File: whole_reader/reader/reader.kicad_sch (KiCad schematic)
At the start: 59 parts, among them J1 Speaker+, J2 Speaker-, J3 Conn_02x05_Odd_Even, J4 USB_C_Receptacle_USB2.0_14P, J5 RFID RC522, J6 6P6C, SW1 SW_SPDT, SW2 SW_SPDT, U1 LM386, U2 STM32F103C8T6, U3 MCP16301Hx-xCH, U4 MAX3232, Y1 16MHz

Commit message: minor changes in pcb layout
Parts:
- removed LED1, LED2: KAA-3528SRSGS, LED_SMD:LED_PLCC-2_3x2mm_KA, symbol deadlock-reader-eagle-import:KAA-3528SRSGS
- added D7, D8: LED_Dual_AKA, LED_SMD:LED_Kingbright_KPA-3010_3x2x1mm, symbol Device:LED_Dual_AKA
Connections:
- net GND: now also D7.2 (K), D8.2 (K)
- net at R4.2: now also D7.1 (A1)
- net at R5.2: now also D7.3 (A2)
- net at R6.2: now also D8.1 (A1)
- net at R7.2: now also D8.3 (A2)

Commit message: updates of board
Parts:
- removed D4: BAT60A, Diode_SMD:D_SOD-323, symbol Device:D_Schottky_Dual_CommonAnode_AKK_Split
- added D4: BAT60A, Diode_SMD:D_SOD-323, symbol Diode:BAT60A
- U1: footprint Package_SO:MSOP-8-1EP_3x3mm_P0.65mm_EP1.73x1.85mm_ThermalVias -> Package_SO:SOIC-8_3.9x4.9mm_P1.27mm
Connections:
- net V+: now also D4.1 (K)
- net at J4.A4 (VBUS), J4.A9 (VBUS), J4.B4 (VBUS)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: now also D4.2 (A)
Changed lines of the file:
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@@
 	)
 	(junction
-		(at 212.09 157.48)
-		(diameter 0)
-		(color 0 0 0 0)
-	)
-	(junction
 		(at 238.76 45.72)
 		(diameter 0)
@@
 	(wire
 		(pts
-			(xy 222.25 157.48) (xy 212.09 157.48)
+			(xy 196.85 157.48) (xy 222.25 157.48)
 		)
 		(stroke
@@
 	(wire
 		(pts
-			(xy 212.09 157.48) (xy 196.85 157.48)
-		)
-		(stroke
-			(width 0)
-			(type default)
-		)
-	)
-	(wire
-		(pts
 			(xy 173.99 147.32) (xy 173.99 132.08)
 		)
@@
 			)
 		)
-		(property "Footprint" "Package_SO:MSOP-8-1EP_3x3mm_P0.65mm_EP1.73x1.85mm_ThermalVias"
+		(property "Footprint" "Package_SO:SOIC-8_3.9x4.9mm_P1.27mm"
 			(at 53.34 36.83 0)
 			(effects
@@
 	)
 	(symbol
+		(lib_id "Diode:BAT60A")
+		(at 226.06 157.48 0)
+		(unit 1)
+		(exclude_from_sim no)
+		(in_bom yes)
+		(on_board yes)
+		(dnp no)
+		(fields_autoplaced yes)
+		(property "Reference" "D4"
+			(at 225.7425 151.13 0)
+			(effects
+				(font
+					(size 1.27 1.27)
+				)
+			)
+		)
+		(property "Value" "BAT60A"
+			(at 225.7425 153.67 0)
+			(effects
+				(font
+					(size 1.27 1.27)
+				)
+			)
+		)
+		(property "Footprint" "Diode_SMD:D_SOD-323"
+			(at 226.06 161.925 0)
+			(effects
+				(font
+					(size 1.27 1.27)
+				)
+				(hide yes)
+			)
+		)
+		(property "Datasheet" "https://www.infineon.com/dgdl/Infineon-BAT60ASERIES-DS-v01_01-en.pdf?fileId=db3a304313d846880113def70c9304a9"
+			(at 226.06 157.48 0)
+			(effects
+				(font
+					(size 1.27 1.27)
+				)
+				(hide yes)
+			)
+		)
+		(property "Description" "10V 3A High Current Recitifier Schottky Diode, SOD-323"
+			(at 226.06 157.48 0)
+			(effects
+				(font
+					(size 1.27 1.27)
+				)
+				(hide yes)
+			)
+		)
+		(pin "2"
+		)
+		(pin "1"
+		)
+		(instances
+			(project ""
+				(path "/6275a1a7-d424-4390-b849-2e49b1a9780b"
+					(reference "D4")
+					(unit 1)
+				)
+			)
+		)
+	)
+	(symbol
 		(lib_id "Device:C")
 		(at 209.55 38.1 0)
@@
 	)
 	(symbol
-		(lib_id "power:PWR_FLAG")
-		(at 212.09 157.48 0)
-		(unit 1)
-		(exclude_from_sim no)
-		(in_bom yes)
-		(on_board yes)
-		(dnp no)
-		(fields_autoplaced yes)
-		(property "Reference" "#FLG04"
-			(at 212.09 155.575 0)
-			(effects
-				(font
-					(size 1.27 1.27)
-				)
-				(hide yes)
-			)
-		)
-		(property "Value" "PWR_FLAG"
-			(at 212.09 152.4 0)
-			(effects
-				(font
-					(size 1.27 1.27)
-				)
-			)
-		)
-		(property "Footprint" ""
-			(at 212.09 157.48 0)
-			(effects
-				(font
-					(size 1.27 1.27)
-				)
-				(hide yes)
-			)
-		)
-		(property "Datasheet" "~"
-			(at 212.09 157.48 0)
-			(effects
-				(font
-					(size 1.27 1.27)
-				)
-				(hide yes)
-			)
-		)
-		(property "Description" "Special symbol for telling ERC where power comes from"
-			(at 212.09 157.48 0)
-			(effects
-				(font
-					(size 1.27 1.27)
-				)
-				(hide yes)
-			)
-		)
-		(pin "1"
-		)
-		(instances
-			(project "reader"
-				(path "/6275a1a7-d424-4390-b849-2e49b1a9780b"
-					(reference "#FLG04")
-					(unit 1)
-				)
-			)
-		)
-	)
-	(symbol
 		(lib_id "power:GND")
 		(at 241.3 106.68 0)
@@
 					(unit 1)
 				)
-			)
-		)
-	)
-	(symbol
-		(lib_id "Device:D_Schottky_Dual_CommonAnode_AKK_Split")
-		(at 226.06 157.48 180)
-		(unit 1)
-		(exclude_from_sim no)
-		(in_bom yes)
-		(on_board yes)
-		(dnp no)
-		(fields_autoplaced yes)
-		(property "Reference" "D4"
-			(at 225.806 152.4 0)
-			(effects
-				(font
-					(size 1.27 1.27)
-				)
-			)
-		)
-		(property "Value" "BAT60A"
-			(at 225.806 154.94 0)
-			(effects
-				(font
-					(size 1.27 1.27)
-				)
-			)
-		)
-		(property "Footprint" "Diode_SMD:D_SOD-323"
-			(at 228.6 154.94 0)
-			(effects
-				(font
-					(size 1.27 1.27)
-				)
-				(hide yes)
-			)
-		)
-		(property "Datasheet" "~"
-			(at 228.6 154.94 0)
-			(effects
-				(font
-					(size 1.27 1.27)
-				)
-				(hide yes)
-			)
-		)
-		(property "Description" "Dual Schottky diode, common anode on pin 1"
-			(at 226.06 157.48 0)
-			(effects
-				(font
-					(size 1.27 1.27)
-				)
-				(hide yes)
-			)
-		)
-		(pin "2"
-		)
-		(pin "3"
-		)
-		(pin "1"
-		)
-		(instances
-			(project "reader"
-				(path "/6275a1a7-d424-4390-b849-2e49b1a9780b"
-					(reference "D4")
-					(unit 1)
-				)

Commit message: trying adding solder pads
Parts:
- J3: footprint Connector_PinHeader_1.27mm:PinHeader_2x05_P1.27mm_Vertical_SMD -> Connector_PinHeader_2.54mm:PinHeader_1x06_P2.54mm_Vertical; symbol Connector_Generic:Conn_02x05_Odd_Even -> Connector:Conn_01x06_Socket
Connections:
- net GND: now also J3.6 (Pin_6); no longer J3.3 (Pin_3), J3.5 (Pin_5), J3.9 (Pin_9)
- net RST: now also J3.5 (Pin_5); no longer J3.10 (Pin_10)
- net SWCLK: now also J3.3 (Pin_3); no longer J3.4 (Pin_4)
- net TRACESWO: now also J3.4 (Pin_4); no longer J3.6 (Pin_6)
- no-connect marks 28 -> 26
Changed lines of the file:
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@@
 	)
 	(junction
-		(at 196.85 101.6)
-		(diameter 0)
-		(color 0 0 0 0)
-	)
-	(junction
 		(at 233.68 29.21)
 		(diameter 0)
@@
 		(color 0 0 0 0)
 	)
-	(junction
-		(at 196.85 106.68)
-		(diameter 0)
-		(color 0 0 0 0)
-	)
 	(no_connect
 		(at 90.17 130.81)
@@
 	)
 	(no_connect
-		(at 203.2 104.14)
-	)
-	(no_connect
 		(at 90.17 125.73)
 	)
@@
 	)
 	(no_connect
-		(at 215.9 104.14)
-	)
-	(no_connect
 		(at 204.47 74.93)
 	)
@@
 	(wire
 		(pts
-			(xy 196.85 101.6) (xy 203.2 101.6)
-		)
-		(stroke
-			(width 0)
-			(type default)
-		)
-	)
-	(wire
-		(pts
 			(xy 48.26 26.67) (xy 48.26 31.75)
 		)
@@
 	(wire
 		(pts
-			(xy 196.85 106.68) (xy 196.85 107.95)
-		)
-		(stroke
-			(width 0)
-			(type default)
-		)
-	)
-	(wire
-		(pts
 			(xy 264.16 50.8) (xy 232.41 50.8)
 		)
@@
 	(wire
 		(pts
-			(xy 196.85 106.68) (xy 203.2 106.68)
-		)
-		(stroke
-			(width 0)
-			(type default)
-		)
-	)
-	(wire
-		(pts
 			(xy 238.76 45.72) (xy 233.68 45.72)
 		)
@@
 	(wire
 		(pts
-			(xy 229.87 119.38) (xy 215.9 119.38)
+			(xy 194.31 109.22) (xy 194.31 113.03)
 		)
 		(stroke
@@
 	(wire
 		(pts
-			(xy 80.01 83.82) (xy 80.01 85.09)
+			(xy 229.87 119.38) (xy 215.9 119.38)
 		)
 		(stroke
@@
 	(wire
 		(pts
-			(xy 35.56 31.75) (xy 35.56 33.02)
+			(xy 80.01 83.82) (xy 80.01 85.09)
 		)
 		(stroke
@@
 	(wire
 		(pts
-			(xy 154.94 153.67) (xy 147.32 153.67)
+			(xy 35.56 31.75) (xy 35.56 33.02)
 		)
 		(stroke
@@
 	(wire
 		(pts
-			(xy 165.1 187.96) (xy 165.1 186.69)
+			(xy 154.94 153.67) (xy 147.32 153.67)
 		)
 		(stroke
@@
 	(wire
 		(pts
-			(xy 241.3 100.33) (xy 241.3 106.68)
+			(xy 165.1 187.96) (xy 165.1 186.69)
 		)
 		(stroke
@@
 	(wire
 		(pts
-			(xy 90.17 86.36) (xy 80.01 86.36)
+			(xy 241.3 100.33) (xy 241.3 106.68)
 		)
 		(stroke
@@
 	(wire
 		(pts
-			(xy 130.81 26.67) (xy 130.81 35.56)
+			(xy 90.17 86.36) (xy 80.01 86.36)
 		)
 		(stroke
@@
 	(wire
 		(pts
-			(xy 196.85 99.06) (xy 196.85 101.6)
+			(xy 130.81 26.67) (xy 130.81 35.56)
 		)
 		(stroke
@@
 	(wire
 		(pts
-			(xy 203.2 99.06) (xy 196.85 99.06)
-		)
-		(stroke
-			(width 0)
-			(type default)
-		)
-	)
-	(wire
-		(pts
 			(xy 68.58 60.96) (xy 68.58 67.31)
 		)
@@
 	(wire
 		(pts
+			(xy 203.2 109.22) (xy 194.31 109.22)
+		)
+		(stroke
+			(width 0)
+			(type default)
+		)
+	)
+	(wire
+		(pts
 			(xy 165.1 147.32) (xy 173.99 147.32)
 		)
@@
 	(wire
 		(pts
-			(xy 196.85 101.6) (xy 196.85 106.68)
-		)
-		(stroke
-			(width 0)
-			(type default)
-		)
-	)
-	(wire
-		(pts
 			(xy 257.81 67.31) (xy 257.81 72.39)
 		)
@@
 	(global_label "TRACESWO"
 		(shape input)
-		(at 215.9 101.6 0)
+		(at 203.2 104.14 180)
 		(fields_autoplaced yes)
 		(effects
@@
 				(size 1.27 1.27)
 			)
-			(justify left)
+			(justify right)
 		)
 		(property "Intersheetrefs" "${INTERSHEET_REFS}"
-			(at 228.6218 101.6 0)
+			(at 190.4782 104.14 0)
 			(effects
 				(font
 					(size 1.27 1.27)
 				)
-				(justify left)
+				(justify right)
 				(hide yes)
 			)
@@
 	(global_label "SWCLK"
 		(shape input)
-		(at 215.9 99.06 0)
+		(at 203.2 101.6 180)
 		(fields_autoplaced yes)
 		(effects
@@
 				(size 1.27 1.27)
 			)
-			(justify left)
+			(justify right)
 		)
 		(property "Intersheetrefs" "${INTERSHEET_REFS}"
-			(at 225.1142 99.06 0)
+			(at 193.9858 101.6 0)
 			(effects
 				(font
 					(size 1.27 1.27)
 				)
-				(justify left)
+				(justify right)
 				(hide yes)
 			)
@@
 	(global_label "SWDIO"
 		(shape input)
-		(at 215.9 96.52 0)
+		(at 203.2 99.06 180)
 		(fields_autoplaced yes)
 		(effects
@@
 				(size 1.27 1.27)
 			)
-			(justify left)
+			(justify right)
 		)
 		(property "Intersheetrefs" "${INTERSHEET_REFS}"
-			(at 224.7514 96.52 0)
+			(at 194.3486 99.06 0)
 			(effects
 				(font
 					(size 1.27 1.27)
 				)
-				(justify left)
+				(justify right)
 				(hide yes)
 			)
@@
 	(global_label "RST"
 		(shape input)
-		(at 215.9 106.68 0)
+		(at 203.2 106.68 180)
 		(fields_autoplaced yes)
 		(effects
@@
 				(size 1.27 1.27)
 			)
-			(justify left)
+			(justify right)
 		)
 		(property "Intersheetrefs" "${INTERSHEET_REFS}"
-			(at 222.3323 106.68 0)
+			(at 196.7677 106.68 0)
 			(effects
 				(font
 					(size 1.27 1.27)
 				)
-				(justify left)
+				(justify right)
 				(hide yes)
 			)
@@
 	)
 	(symbol
-		(lib_id "Connector_Generic:Conn_02x05_Odd_Even")
+		(lib_id "Connector:Conn_01x06_Socket")
 		(at 208.28 101.6 0)
 		(unit 1)
@@
 		(fields_autoplaced yes)
 		(property "Reference" "J3"
-			(at 209.55 90.17 0)
+			(at 209.55 101.5999 0)
 			(effects
 				(font
 					(size 1.27 1.27)
 				)
+				(justify left)
 			)
 		)
 		(property "Value" "Conn_02x05_Odd_Even"
-			(at 209.55 92.71 0)
+			(at 209.55 104.1399 0)
 			(effects
 				(font
 					(size 1.27 1.27)
 				)
+				(justify left)
 			)
 		)
-		(property "Footprint" "Connector_PinHeader_1.27mm:PinHeader_2x05_P1.27mm_Vertical_SMD"
+		(property "Footprint" "Connector_PinHeader_2.54mm:PinHeader_1x06_P2.54mm_Vertical"
 			(at 208.28 101.6 0)
 			(effects
@@
 			)
 		)
-		(property "Description" "Generic connector, double row, 02x05, odd/even pin numbering scheme (row 1 odd numbers, row 2 even numbers), script generated (kicad-library-utils/schlib/autogen/connector/)"
+		(property "Description" "Generic connector, single row, 01x06, script generated"
 			(at 208.28 101.6 0)
 			(effects
@@
 		(pin "5"
 		)
-		(pin "7"
-		)
-		(pin "10"
-		)
-		(pin "8"
-		)
 		(pin "3"
 		)
-		(pin "9"
-		)
 		(instances
 			(project "reader"
@@
 	)
 	(symbol
-		(lib_id "power:GND")
-		(at 196.85 107.95 0)
-		(unit 1)
-		(exclude_from_sim no)
-		(in_bom yes)
-		(on_board yes)
-		(dnp no)
-		(fields_autoplaced yes)
-		(property "Reference" "#PWR033"
-			(at 196.85 114.3 0)
-			(effects
-				(font
-					(size 1.27 1.27)
-				)
-				(hide yes)
-			)
-		)
-		(property "Value" "GND"
-			(at 196.85 113.03 0)
-			(effects
-				(font
-					(size 1.27 1.27)
-				)
-			)
-		)
-		(property "Footprint" ""
-			(at 196.85 107.95 0)
-			(effects
-				(font
-					(size 1.27 1.27)
-				)
-				(hide yes)
-			)
-		)
-		(property "Datasheet" ""
-			(at 196.85 107.95 0)
-			(effects
-				(font
-					(size 1.27 1.27)
-				)
-				(hide yes)
-			)
-		)
-		(property "Description" "Power symbol creates a global label with name \"GND\" , ground"
-			(at 196.85 107.95 0)
-			(effects
-				(font
-					(size 1.27 1.27)
-				)
-				(hide yes)
-			)
-		)
-		(pin "1"
-		)
-		(instances
-			(project "reader"
-				(path "/6275a1a7-d424-4390-b849-2e49b1a9780b"
-					(reference "#PWR033")
-					(unit 1)
-				)
-			)
-		)
-	)
-	(symbol
 		(lib_id "Connector:Conn_01x01_Socket")
 		(at 83.82 55.88 90)
@@
 					(unit 1)
 				)
+			)
+		)
+	)
+	(symbol
+		(lib_id "power:GND")
+		(at 194.31 113.03 0)
+		(unit 1)
+		(exclude_from_sim no)
+		(in_bom yes)
+		(on_board yes)
+		(dnp no)
+		(fields_autoplaced yes)
+		(property "Reference" "#PWR033"
+			(at 194.31 119.38 0)
+			(effects
+				(font
+					(size 1.27 1.27)
+				)
+				(hide yes)
+			)
+		)
+		(property "Value" "GND"
+			(at 194.31 118.11 0)
+			(effects
+				(font
+					(size 1.27 1.27)
+				)
+			)
+		)
+		(property "Footprint" ""
+			(at 194.31 113.03 0)
+			(effects
+				(font
+					(size 1.27 1.27)
+				)
+				(hide yes)
+			)
+		)
+		(property "Datasheet" ""
+			(at 194.31 113.03 0)
+			(effects
+				(font
+					(size 1.27 1.27)
+				)
+				(hide yes)
+			)
+		)
+		(property "Description" "Power symbol creates a global label with name \"GND\" , ground"
+			(at 194.31 113.03 0)
+			(effects
+				(font
+					(size 1.27 1.27)
+				)
+				(hide yes)
+			)
+		)
+		(pin "1"
+		)
+		(instances
+			(project ""
+				(path "/6275a1a7-d424-4390-b849-2e49b1a9780b"
+					(reference "#PWR033")
+					(unit 1)
+				)

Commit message: updating footprint
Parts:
- J1, J2: footprint Connector_Wire:SolderWirePad_1x01_SMD_1x2mm -> Connector_PinSocket_2.00mm:PinSocket_1x01_P2.00mm_Vertical
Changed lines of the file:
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@@
 			)
 		)
-		(property "Footprint" "Connector_Wire:SolderWirePad_1x01_SMD_1x2mm"
+		(property "Footprint" "Connector_PinSocket_2.00mm:PinSocket_1x01_P2.00mm_Vertical"
 			(at 83.82 52.07 0)
 			(effects
@@
 			)
 		)
-		(property "Footprint" "Connector_Wire:SolderWirePad_1x01_SMD_1x2mm"
+		(property "Footprint" "Connector_PinSocket_2.00mm:PinSocket_1x01_P2.00mm_Vertical"
 			(at 83.82 55.88 0)
 			(effects

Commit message: Úprava PCB a schémy zapojenia
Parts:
- D1: Note ? -> (none)
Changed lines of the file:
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@@
 (kicad_sch
-	(version 20231120)
+	(version 20250114)
 	(generator "eeschema")
-	(generator_version "8.0")
+	(generator_version "9.0")
 	(paper "A4")
+	(text_box "Nechýba tu pripojenie RC522 na napájanie"
+		(exclude_from_sim no)
+		(at 267.97 82.55 0)
+		(size 13.97 10.16)
+		(margins 0.9525 0.9525 0.9525 0.9525)
+		(stroke
+			(width 0)
+			(type solid)
+		)
+		(fill
+			(type none)
+		)
+		(effects
+			(font
+				(size 1.27 1.27)
+			)
+			(justify left top)
+		)
+	)
 	(junction
 		(at 48.26 90.17)
@@
 					(size 1.27 1.27)
 				)
-				(hide yes)
 			)
 		)
@@
 					(size 1.27 1.27)
 				)
-				(hide yes)
 			)
 		)
@@
 			)
 		)
-		(property "Note" "?"
-			(at 140.208 130.81 0)
-			(effects
-				(font
-					(size 1.5 1.5)
-					(bold yes)
-				)
-			)
-		)
 		(pin "1"
 		)
@@
 		(lib_id "Device:R")
 		(at 125.73 39.37 0)
+		(mirror y)
 		(unit 1)
 		(exclude_from_sim no)
@@
 		(dnp no)
 		(property "Reference" "R6"
-			(at 122.936 42.164 90)
+			(at 128.524 42.164 90)
 			(effects
 				(font
@@
 		)
 		(property "Value" "330R"
-			(at 122.936 37.846 90)
+			(at 128.524 37.846 90)
 			(effects
 				(font
@@
 		)
 		(property "Footprint" "Resistor_SMD:R_0402_1005Metric"
-			(at 123.952 39.37 90)
+			(at 127.508 39.37 90)
 			(effects
 				(font
@@
 		)
 	)
+	(embedded_fonts no)
 )

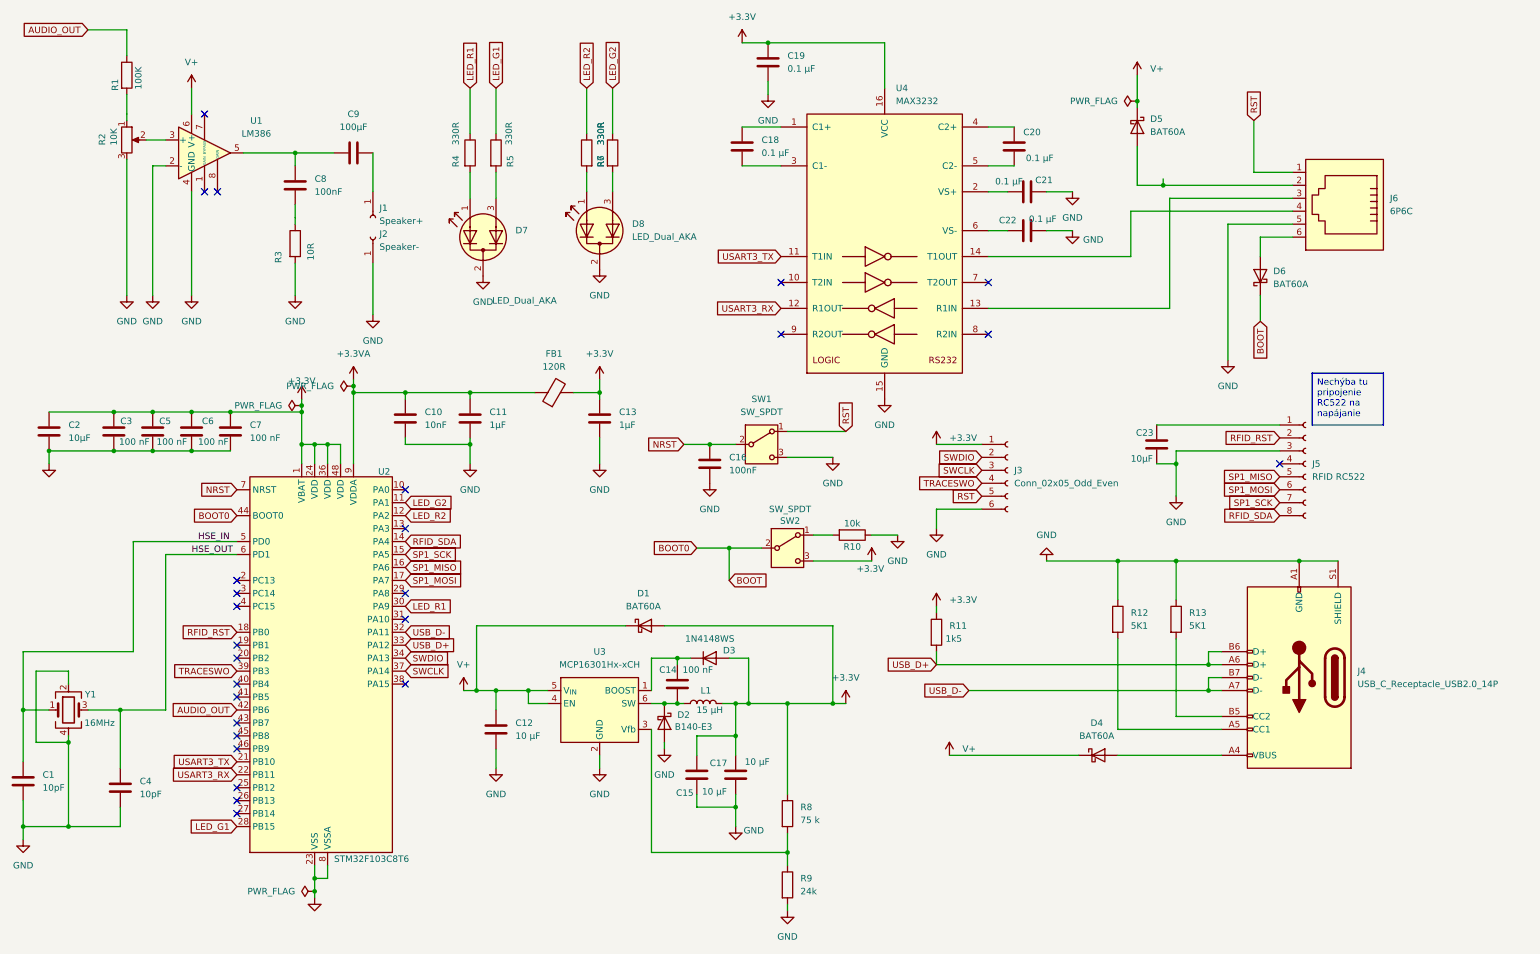
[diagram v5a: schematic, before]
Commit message: updates to pcb and added some 3d models
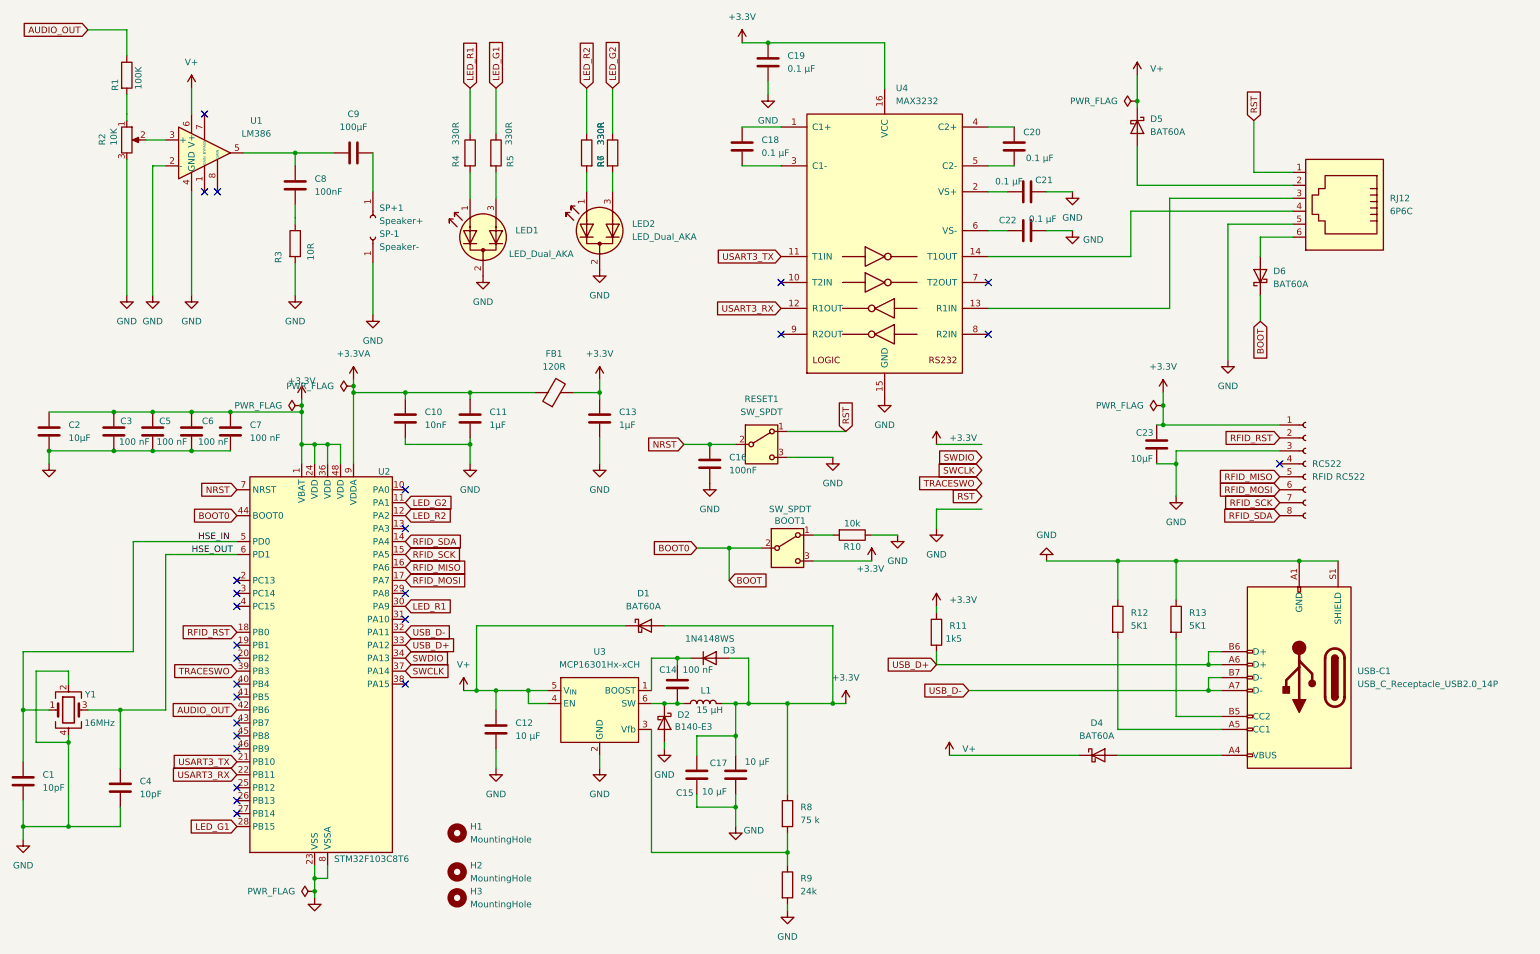
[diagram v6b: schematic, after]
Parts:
- removed J3: Conn_02x05_Odd_Even, Connector_PinHeader_2.54mm:PinHeader_1x06_P2.54mm_Vertical, symbol Connector:Conn_01x06_Socket
- added H1, H2, H3: MountingHole, MountingHole:MountingHole_2.2mm_M2, symbol Mechanical:MountingHole
- SP+1: renamed from J1; footprint Connector_PinSocket_2.00mm:PinSocket_1x01_P2.00mm_Vertical -> Connector_Wire:SolderWire-0.1sqmm_1x01_D0.4mm_OD1mm
- SP-1: renamed from J2; footprint Connector_PinSocket_2.00mm:PinSocket_1x01_P2.00mm_Vertical -> Connector_Wire:SolderWire-0.1sqmm_1x01_D0.4mm_OD1mm
- renumbered SW2 to BOOT1, D7 to LED1, D8 to LED2, J5 to RC522, SW1 to RESET1, J6 to RJ12, J4 to USB-C1
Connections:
- net +3.3V: now also C23.1, RC522.1 (Pin_1)
- net SP1_MISO renamed RFID_MISO
- net SP1_MOSI renamed RFID_MOSI
- net SP1_SCK renamed RFID_SCK
